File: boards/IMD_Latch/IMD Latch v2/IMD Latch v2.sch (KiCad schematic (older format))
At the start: 15 parts, among them J1 micromatch_female_RA_8, J2 Ultrafit_2, K1 G5Q-1A4-DC5-5V, Q1 SSM3K333R, U1 CD4043BPWR

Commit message: pull down for IMD output
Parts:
- added R?: R_2.2k, footprints:R_0805_OEM, symbol R_2.2k
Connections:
- net GND: now also R?.2
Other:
- note added: "IMD Output"
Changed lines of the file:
@@
 	1    0    0    -1
 $EndComp
+$Comp
+L R_2.2k R?
+U 1 1 5A077434
+P 4950 3850
+F 0 "R?" V 5030 3850 50  0000 C CNN
+F 1 "R_2.2k" V 4850 3850 50  0000 C CNN
+F 2 "footprints:R_0805_OEM" H 4880 3850 50  0001 C CNN
+F 3 "https://www.seielect.com/Catalog/SEI-RMCF_RMCP.pdf" H 5030 3850 50  0001 C CNN
+F 4 "RMCF0805FT2K20CT-ND" H 4950 3850 60  0001 C CNN "MPN"
+F 5 "Digi-Key" H 4950 3850 60  0001 C CNN "MFN"
+F 6 "Value" H 4950 3850 60  0001 C CNN "Package"
+F 7 "https://www.digikey.com/product-detail/en/stackpole-electronics-inc/RMCF0805FT2K20/RMCF0805FT2K20CT-ND/1942387" H 5430 4250 60  0001 C CNN "PurchasingLink"
+	1    4950 3850
+	1    0    0    -1
+$EndComp
+$Comp
+L GND #PWR?
+U 1 1 5A077481
+P 4950 4000
+F 0 "#PWR?" H 4950 3750 50  0001 C CNN
+F 1 "GND" H 4950 3850 50  0000 C CNN
+F 2 "" H 4950 4000 50  0001 C CNN
+F 3 "" H 4950 4000 50  0001 C CNN
+	1    4950 4000
+	1    0    0    -1
+$EndComp
+Text Notes 3950 3700 0    60   ~ 0
+IMD Output
 $EndSCHEMATC

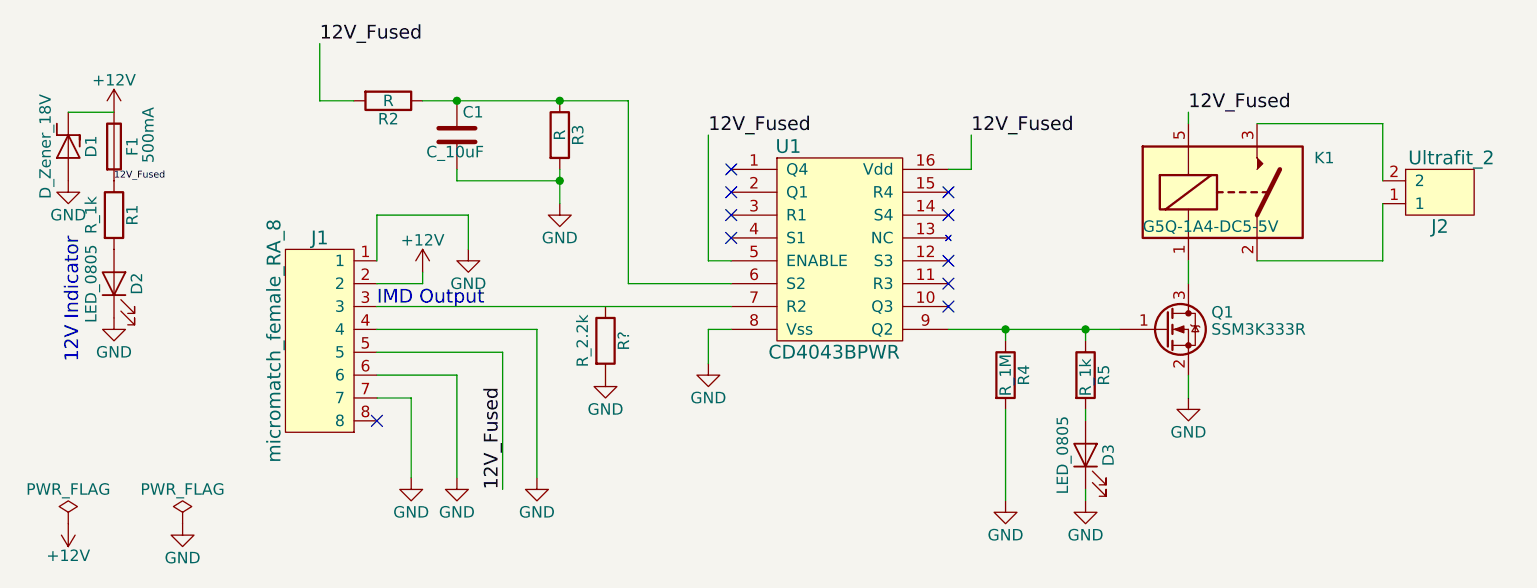
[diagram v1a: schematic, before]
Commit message: IMD Latch V2 Layout
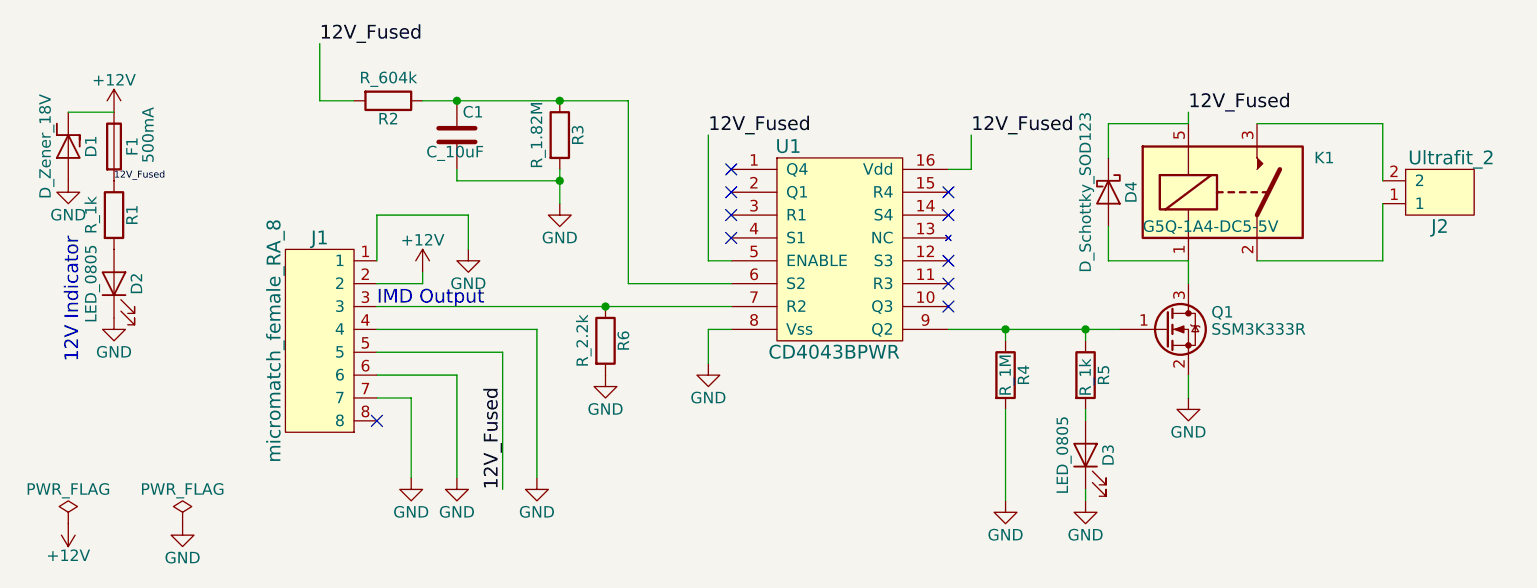
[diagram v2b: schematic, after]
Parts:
- removed R2, R3: R, symbol R
- added D4: D_Schottky_SOD123, footprints:D_SOD-123W_OEM, symbol D_Schottky_SOD123
- added R2: R_604k, footprints:R_0805_OEM, symbol R_604k
- added R3: R_1.82M, footprints:R_0805_OEM, symbol R_1.82M
- D2: footprint LEDs:LED_0805 -> footprints:LED_0805_OEM
- R1: footprint Resistors_SMD:R_0805 -> footprints:R_0805_OEM
- gave numbers to parts that had none: 1
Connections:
- net 12V_Fused: now also D4.1 (K), R2.2
- net GND: now also R3.2
- net at C1.1, U1.6 (S2): now also R2.1, R3.1
- net at J1.3, U1.7 (R2): now also R6.1
- net at K1.1, Q1.3 (D): now also D4.2 (A)
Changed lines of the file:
@@
 F 0 "R1" V 2880 3300 50  0000 C CNN
 F 1 "R_1k" V 2700 3300 50  0000 C CNN
-F 2 "Resistors_SMD:R_0805" H 2730 3300 50  0001 C CNN
+F 2 "footprints:R_0805_OEM" H 2730 3300 50  0001 C CNN
 F 3 "https://www.seielect.com/Catalog/SEI-rncp.pdf" H 2880 3300 50  0001 C CNN
 F 4 "Digi-Key" H 2800 3300 60  0001 C CNN "MFN"
@@
 F 0 "D2" H 2800 3500 50  0000 C CNN
 F 1 "LED_0805" H 2800 3700 50  0000 C CNN
-F 2 "LEDs:LED_0805" H 2700 3600 50  0001 C CNN
+F 2 "footprints:LED_0805_OEM" H 2700 3600 50  0001 C CNN
 F 3 "http://www.osram-os.com/Graphics/XPic9/00078860_0.pdf" H 2800 3700 50  0001 C CNN
 F 4 "475-1410-1-ND" H 2800 3600 60  0001 C CNN "MPN"
@@
 $EndComp
 $Comp
-L +12V #PWR01
+L +12V #PWR3
 U 1 1 59E04C1A
 P 2800 2850
-F 0 "#PWR01" H 2800 2700 50  0001 C CNN
+F 0 "#PWR3" H 2800 2700 50  0001 C CNN
 F 1 "+12V" H 2800 2990 50  0000 C CNN
 F 2 "" H 2800 2850 50  0001 C CNN
@@
 $EndComp
 $Comp
-L GND #PWR02
+L GND #PWR4
 U 1 1 59E0588D
 P 2800 3750
-F 0 "#PWR02" H 2800 3500 50  0001 C CNN
+F 0 "#PWR4" H 2800 3500 50  0001 C CNN
 F 1 "GND" H 2800 3600 50  0000 C CNN
 F 2 "" H 2800 3750 50  0001 C CNN
@@
 $EndComp
 $Comp
-L PWR_FLAG #FLG03
+L PWR_FLAG #FLG1
 U 1 1 59E0A741
 P 2600 4650
-F 0 "#FLG03" H 2600 4725 50  0001 C CNN
+F 0 "#FLG1" H 2600 4725 50  0001 C CNN
 F 1 "PWR_FLAG" H 2600 4800 50  0000 C CNN
 F 2 "" H 2600 4650 50  0001 C CNN
@@
 $EndComp
 $Comp
-L PWR_FLAG #FLG04
+L PWR_FLAG #FLG2
 U 1 1 59E0A7A5
 P 3100 4650
-F 0 "#FLG04" H 3100 4725 50  0001 C CNN
+F 0 "#FLG2" H 3100 4725 50  0001 C CNN
 F 1 "PWR_FLAG" H 3100 4800 50  0000 C CNN
 F 2 "" H 3100 4650 50  0001 C CNN
@@
 $EndComp
 $Comp
-L +12V #PWR05
+L +12V #PWR2
 U 1 1 59E0A7D7
 P 2600 4650
-F 0 "#PWR05" H 2600 4500 50  0001 C CNN
+F 0 "#PWR2" H 2600 4500 50  0001 C CNN
 F 1 "+12V" H 2600 4790 50  0000 C CNN
 F 2 "" H 2600 4650 50  0001 C CNN
@@
 $EndComp
 $Comp
-L GND #PWR06
+L GND #PWR5
 U 1 1 59E0A859
 P 3100 4650
-F 0 "#PWR06" H 3100 4400 50  0001 C CNN
+F 0 "#PWR5" H 3100 4400 50  0001 C CNN
 F 1 "GND" H 3100 4500 50  0000 C CNN
 F 2 "" H 3100 4650 50  0001 C CNN
@@
 $EndComp
 $Comp
-L GND #PWR07
+L GND #PWR1
 U 1 1 59F277D6
 P 2600 3150
-F 0 "#PWR07" H 2600 2900 50  0001 C CNN
+F 0 "#PWR1" H 2600 2900 50  0001 C CNN
 F 1 "GND" H 2600 3000 50  0000 C CNN
 F 2 "" H 2600 3150 50  0001 C CNN
@@
 $EndComp
 $Comp
-L +12V #PWR08
+L +12V #PWR7
 U 1 1 5A028E2B
 P 4150 3550
-F 0 "#PWR08" H 4150 3400 50  0001 C CNN
+F 0 "#PWR7" H 4150 3400 50  0001 C CNN
 F 1 "+12V" H 4150 3690 50  0000 C CNN
 F 2 "" H 4150 3550 50  0001 C CNN
@@
 $EndComp
 $Comp
-L GND #PWR09
+L GND #PWR6
 U 1 1 5A028E67
 P 4100 4450
-F 0 "#PWR09" H 4100 4200 50  0001 C CNN
+F 0 "#PWR6" H 4100 4200 50  0001 C CNN
 F 1 "GND" H 4100 4300 50  0000 C CNN
 F 2 "" H 4100 4450 50  0001 C CNN
@@
 $EndComp
 $Comp
-L GND #PWR010
+L GND #PWR8
 U 1 1 5A028F0E
 P 4300 4450
-F 0 "#PWR010" H 4300 4200 50  0001 C CNN
+F 0 "#PWR8" H 4300 4200 50  0001 C CNN
 F 1 "GND" H 4300 4300 50  0000 C CNN
 F 2 "" H 4300 4450 50  0001 C CNN
@@
 $EndComp
 $Comp
-L GND #PWR011
+L GND #PWR10
 U 1 1 5A028F4A
 P 4650 4450
-F 0 "#PWR011" H 4650 4200 50  0001 C CNN
+F 0 "#PWR10" H 4650 4200 50  0001 C CNN
 F 1 "GND" H 4650 4300 50  0000 C CNN
 F 2 "" H 4650 4450 50  0001 C CNN
@@
 12V_Fused
 $Comp
-L GND #PWR012
+L GND #PWR9
 U 1 1 5A02994C
 P 4350 3450
-F 0 "#PWR012" H 4350 3200 50  0001 C CNN
+F 0 "#PWR9" H 4350 3200 50  0001 C CNN
 F 1 "GND" H 4350 3300 50  0000 C CNN
 F 2 "" H 4350 3450 50  0001 C CNN
@@
 $EndComp
 $Comp
-L GND #PWR013
+L GND #PWR16
 U 1 1 5A02B918
 P 7500 4100
-F 0 "#PWR013" H 7500 3850 50  0001 C CNN
+F 0 "#PWR16" H 7500 3850 50  0001 C CNN
 F 1 "GND" H 7500 3950 50  0000 C CNN
 F 2 "" H 7500 4100 50  0001 C CNN
@@
 $EndComp
 $Comp
-L GND #PWR014
+L GND #PWR13
 U 1 1 5A055F8E
 P 5400 3950
-F 0 "#PWR014" H 5400 3700 50  0001 C CNN
+F 0 "#PWR13" H 5400 3700 50  0001 C CNN
 F 1 "GND" H 5400 3800 50  0000 C CNN
 F 2 "" H 5400 3950 50  0001 C CNN
@@
 $EndComp
 $Comp
-L GND #PWR015
+L GND #PWR15
 U 1 1 5A057A89
 P 7050 4550
-F 0 "#PWR015" H 7050 4300 50  0001 C CNN
+F 0 "#PWR15" H 7050 4300 50  0001 C CNN
 F 1 "GND" H 7050 4400 50  0000 C CNN
 F 2 "" H 7050 4550 50  0001 C CNN
@@
 $EndComp
 $Comp
-L GND #PWR016
+L GND #PWR11
 U 1 1 5A05A2C9
 P 4750 3250
-F 0 "#PWR016" H 4750 3000 50  0001 C CNN
+F 0 "#PWR11" H 4750 3000 50  0001 C CNN
 F 1 "GND" H 4750 3100 50  0000 C CNN
 F 2 "" H 4750 3250 50  0001 C CNN
@@
 $EndComp
 $Comp
-L GND #PWR017
+L GND #PWR14
 U 1 1 5A054F56
 P 6700 4550
-F 0 "#PWR017" H 6700 4300 50  0001 C CNN
+F 0 "#PWR14" H 6700 4300 50  0001 C CNN
 F 1 "GND" H 6700 4400 50  0000 C CNN
 F 2 "" H 6700 4550 50  0001 C CNN
@@
 	1    6700 4550
 	1    0    0    -1
-$EndComp
-$Comp
-L R R3
-U 1 1 5A05653D
-P 4750 2950
-F 0 "R3" V 4830 2950 50  0000 C CNN
-F 1 "R" V 4750 2950 50  0000 C CNN
-F 2 "" V 4680 2950 50  0001 C CNN
-F 3 "" H 4750 2950 50  0001 C CNN
-	1    4750 2950
-	1    0    0    -1
-$EndComp
-$Comp
-L R R2
-U 1 1 5A05664A
-P 4000 2800
-F 0 "R2" V 4080 2800 50  0000 C CNN
-F 1 "R" V 4000 2800 50  0000 C CNN
-F 2 "" V 3930 2800 50  0001 C CNN
-F 3 "" H 4000 2800 50  0001 C CNN
-	1    4000 2800
-	0    1    1    0
 $EndComp
 Text Label 5400 2950 0    60   ~ 0
@@
 	6550 3100 6450 3100
 $Comp
+L R_2.2k R6
+U 1 1 5A077434
+P 4950 3850
+F 0 "R6" V 5030 3850 50  0000 C CNN
+F 1 "R_2.2k" V 4850 3850 50  0000 C CNN
+F 2 "footprints:R_0805_OEM" H 4880 3850 50  0001 C CNN
+F 3 "https://www.seielect.com/Catalog/SEI-RMCF_RMCP.pdf" H 5030 3850 50  0001 C CNN
+F 4 "RMCF0805FT2K20CT-ND" H 4950 3850 60  0001 C CNN "MPN"
+F 5 "Digi-Key" H 4950 3850 60  0001 C CNN "MFN"
+F 6 "Value" H 4950 3850 60  0001 C CNN "Package"
+F 7 "https://www.digikey.com/product-detail/en/stackpole-electronics-inc/RMCF0805FT2K20/RMCF0805FT2K20CT-ND/1942387" H 5430 4250 60  0001 C CNN "PurchasingLink"
+	1    4950 3850
+	1    0    0    -1
+$EndComp
+$Comp
+L GND #PWR12
+U 1 1 5A077481
+P 4950 4000
+F 0 "#PWR12" H 4950 3750 50  0001 C CNN
+F 1 "GND" H 4950 3850 50  0000 C CNN
+F 2 "" H 4950 4000 50  0001 C CNN
+F 3 "" H 4950 4000 50  0001 C CNN
+	1    4950 4000
+	1    0    0    -1
+$EndComp
+Text Notes 3950 3700 0    60   ~ 0
+IMD Output
+$Comp
+L R_604k R2
+U 1 1 5A07892D
+P 4000 2800
+F 0 "R2" V 4080 2800 50  0000 C CNN
+F 1 "R_604k" V 3900 2800 50  0000 C CNN
+F 2 "footprints:R_0805_OEM" H 3930 2800 50  0001 C CNN
+F 3 "https://www.seielect.com/Catalog/SEI-RMCF_RMCP.pdf" H 4080 2800 50  0001 C CNN
+F 4 "Digi-Key" H 4000 2800 60  0001 C CNN "MFN"
+F 5 "RMCF0805FT604KCT-ND" H 4000 2800 60  0001 C CNN "MPN"
+F 6 "Value" H 4000 2800 60  0001 C CNN "Package"
+F 7 "https://www.digikey.com/product-detail/en/stackpole-electronics-inc/RMCF0805FT604K/RMCF0805FT604KCT-ND/4425214" H 4480 3200 60  0001 C CNN "PurchasingLink"
+	1    4000 2800
+	0    1    1    0
+$EndComp
+$Comp
+L R_1.82M R3
+U 1 1 5A07897A
+P 4750 2950
+F 0 "R3" V 4830 2950 50  0000 C CNN
+F 1 "R_1.82M" V 4650 2950 50  0000 C CNN
+F 2 "footprints:R_0805_OEM" H 4680 2950 50  0001 C CNN
+F 3 "https://www.seielect.com/Catalog/SEI-RMCF_RMCP.pdf" H 4830 2950 50  0001 C CNN
+F 4 "Digi-Key" H 4750 2950 60  0001 C CNN "MFN"
+F 5 "RMCF0805FT1M82CT-ND" H 4750 2950 60  0001 C CNN "MPN"
+F 6 "Value" H 4750 2950 60  0001 C CNN "Package"
+F 7 "https://www.digikey.com/product-detail/en/stackpole-electronics-inc/RMCF0805FT1M82/RMCF0805FT1M82CT-ND/2418309" H 5230 3350 60  0001 C CNN "PurchasingLink"
+	1    4750 2950
+	1    0    0    -1
+$EndComp
+Connection ~ 4950 3700
+$Comp
 L CD4043BPWR U1
-U 1 1 5A071673
+U 1 1 5A078803
 P 6000 3400
 F 0 "U1" H 5750 3800 60  0000 C CNN
@@
 $EndComp
 $Comp
-L R_2.2k R?
-U 1 1 5A077434
-P 4950 3850
-F 0 "R?" V 5030 3850 50  0000 C CNN
-F 1 "R_2.2k" V 4850 3850 50  0000 C CNN
-F 2 "footprints:R_0805_OEM" H 4880 3850 50  0001 C CNN
-F 3 "https://www.seielect.com/Catalog/SEI-RMCF_RMCP.pdf" H 5030 3850 50  0001 C CNN
-F 4 "RMCF0805FT2K20CT-ND" H 4950 3850 60  0001 C CNN "MPN"
-F 5 "Digi-Key" H 4950 3850 60  0001 C CNN "MFN"
-F 6 "Value" H 4950 3850 60  0001 C CNN "Package"
-F 7 "https://www.digikey.com/product-detail/en/stackpole-electronics-inc/RMCF0805FT2K20/RMCF0805FT2K20CT-ND/1942387" H 5430 4250 60  0001 C CNN "PurchasingLink"
-	1    4950 3850
-	1    0    0    -1
-$EndComp
-$Comp
-L GND #PWR?
-U 1 1 5A077481
-P 4950 4000
-F 0 "#PWR?" H 4950 3750 50  0001 C CNN
-F 1 "GND" H 4950 3850 50  0000 C CNN
-F 2 "" H 4950 4000 50  0001 C CNN
-F 3 "" H 4950 4000 50  0001 C CNN
-	1    4950 4000
-	1    0    0    -1
-$EndComp
-Text Notes 3950 3700 0    60   ~ 0
-IMD Output
+L D_Schottky_SOD123 D4
+U 1 1 5A07A854
+P 7150 3200
+F 0 "D4" H 7150 3300 50  0000 C CNN
+F 1 "D_Schottky_SOD123" H 7150 3100 50  0000 C CNN
+F 2 "footprints:D_SOD-123W_OEM" H 7050 3200 50  0001 C CNN
+F 3 "https://assets.nexperia.com/documents/data-sheet/PMEG10010ELR.pdf" H 7150 3300 50  0001 C CNN
+F 4 "1727-2394-1-ND" H 7250 3400 60  0001 C CNN "MPN"
+F 5 "Digi-Key" H 7350 3500 60  0001 C CNN "MFN"
+F 6 "https://www.digikey.com/product-detail/en/nexperia-usa-inc/PMEG10010ELRX/1727-2394-1-ND/5436140" H 7450 3600 60  0001 C CNN "PurchasingLink"
+	1    7150 3200
+	0    1    1    0
+$EndComp
+Wire Wire Line
+	7150 3050 7150 2900
+Wire Wire Line
+	7150 2900 7500 2900
+Wire Wire Line
+	7500 3500 7150 3500
+Wire Wire Line
+	7150 3500 7150 3350
 $EndSCHEMATC
